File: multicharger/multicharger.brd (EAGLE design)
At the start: 26 x 52 mm, 26 parts, among them J2 USB-MICROA-AMPHENOL-10118192-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, J3 HEADER-8POS-, P1 TEST-POINT, P2 TEST-POINT, P3 TEST-POINT, P4 TEST-POINT, P5 TEST-POINT, P6 TEST-POINT, U1 MCP73831T-2ACI/OT, U2 MCP73831T-2ACI/OT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

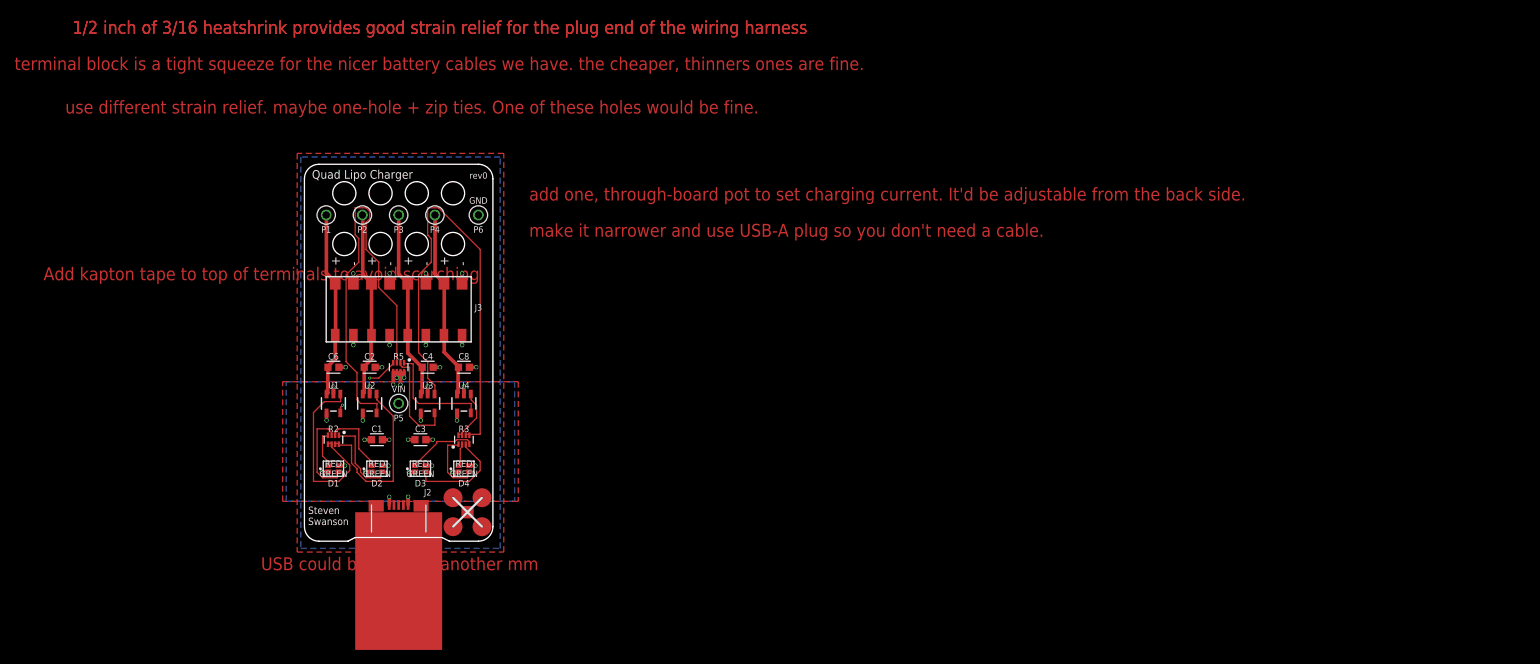
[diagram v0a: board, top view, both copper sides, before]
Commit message: pretty, compact, USB-A version of multicharger
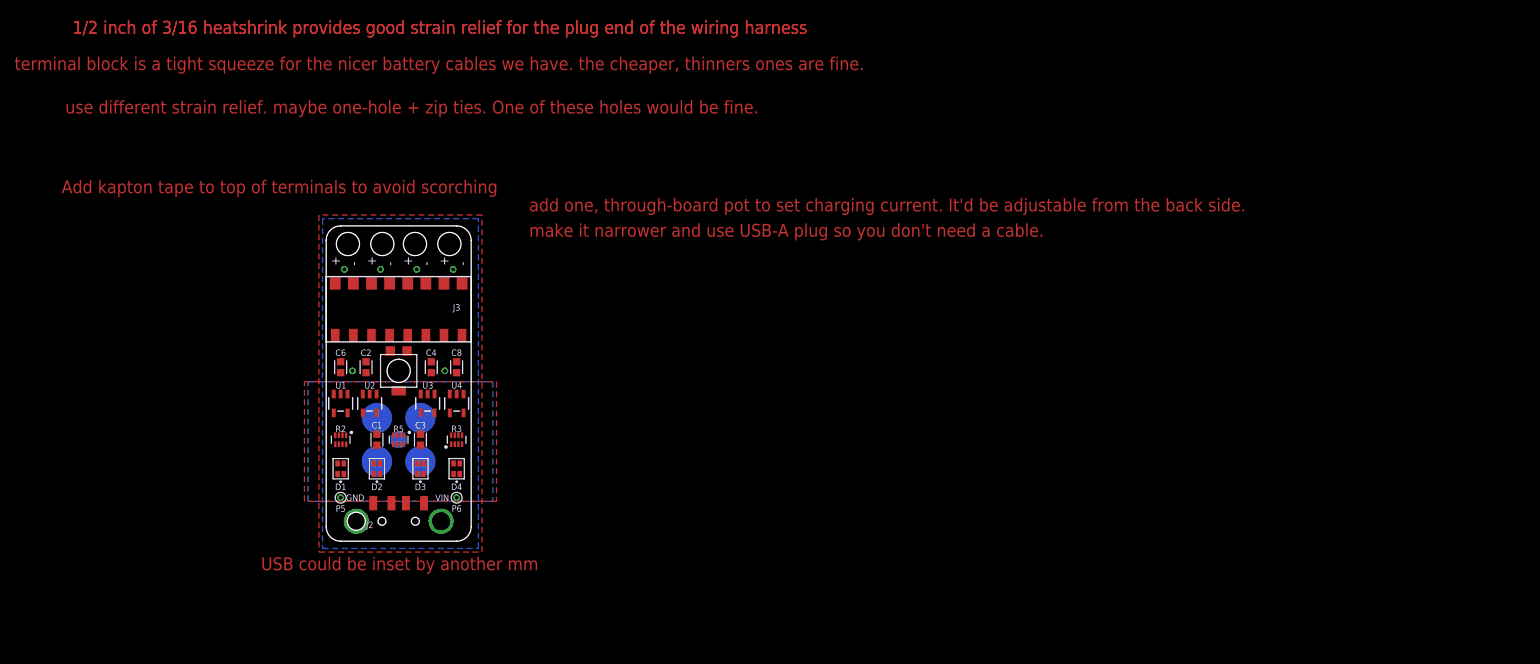
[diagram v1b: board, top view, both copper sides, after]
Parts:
- removed U$1: (no value), quadparts_prebuilt:QUADCLASS_LOGO_SMALL
- added P7: 10K, RemoteParts:BOT-ADJUST-POT-3314R-1-103E
- added P8, P9: TEST-POINT-1MM, RemoteParts:TEST-POINT-1MM-VIA
- added U$2: (no value), quadparts_prebuilt:QUADCLASS_LOGO
- J2: value USB-MICROA-AMPHENOL-10118192-0001LF -> USB-A-SMD-KEYSTONE-931; device RemoteParts:USB-MICROA-10118192-0001LF -> RemoteParts:USB-A-KEYSTONE-931
- P1, P2, P3, P4, P5, P6: value TEST-POINT -> TEST-POINT-1MM; device RemoteParts:TEST-POINT-KEYSTONE-5000 -> RemoteParts:TEST-POINT-1MM-VIA
- moved P6 39.1 mm to (8.00, -16.0)
- moved P5 15.3 mm to (-8.00, -16.0)
- moved R5 10.0 mm to (0.00, -8.00)
- moved P1 7.91 mm to (-7.50, 15.5), flipped to the bottom
- moved P2 7.91 mm to (-2.50, 15.5), flipped to the bottom
- moved P3 7.91 mm to (2.50, 15.5), flipped to the bottom
- moved P4 7.91 mm to (7.50, 15.5), flipped to the bottom
- moved C6 1.00 mm to (-8.00, 2.00), turned to 90 degrees
- moved C8 1.00 mm to (8.00, 2.00), turned to 90 degrees
- moved D1 1.00 mm to (-8.00, -12.0), turned to 270 degrees
- moved D4 1.00 mm to (8.00, -12.0), turned to 270 degrees
- moved J2 1.00 mm to (0.00, -18.0), turned to 180 degrees
- moved R2 1.00 mm to (-8.00, -8.00)
- moved R3 1.00 mm to (8.00, -8.00)
- moved U1 1.00 mm to (-8.00, -3.00)
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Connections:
- new net N$17: P7.1, P8.T
- new net N$18: P7.3, P9.T
- net GND: now also J2.G1, J2.G2; no longer J2.10, J2.11, J2.5, J2.6, J2.7, J2.8, J2.9
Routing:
- net N$7: track 65.0 -> 0.00 mm
- net N$4: track 57.4 -> 0.00 mm
- net GND: track 30.5 -> 0.00 mm, vias 27 -> 0
- net BPOS3: track 26.1 -> 0.00 mm
- net BPOS4: track 26.1 -> 0.00 mm
- net N$11: track 26.0 -> 0.00 mm
- net BPOS1: track 25.7 -> 0.00 mm
- net BPOS2: track 25.7 -> 0.00 mm
- net N$3: track 25.2 -> 0.00 mm
- net N$14: track 15.8 -> 0.00 mm
- net N$8: track 14.2 -> 0.00 mm
- net N$9: track 13.9 -> 0.00 mm
- net N$1: track 12.6 -> 0.00 mm
- net N$5: track 11.7 -> 0.00 mm
- net VIN: track 10.7 -> 0.00 mm, vias 11 -> 0
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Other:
- board size 26 x 52 mm -> 20 x 43.5 mm
- board text added: "1kΩ: 250mA"
- board text added: "250Ω: 1000mA"
- board text added: "500Ω: 500mA"
- board text added: "Set Charging Current"
- board text added: "rev1"
- board text removed: "rev0"
